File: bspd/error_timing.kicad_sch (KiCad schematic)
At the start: 19 parts, among them Q2 XP262N7002TR-G, Q3 BC856, U6 40106

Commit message: Routing
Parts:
- renumbered D6 to D11, D9 to D12, R35 to R36, R31 to R37, R32 to R38, R33 to R39, R36 to R40, R37 to R41, R38 to R42, R39 to R43
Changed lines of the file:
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@@
 		(on_board yes)
 		(dnp no)
-		(property "Reference" "R35"
+		(property "Reference" "R36"
 			(at 61.595 120.015 90)
 			(effects
@@
 			(project "BSPD"
 				(path "/a7fc0812-140f-4d96-9cd8-ead8c1c610b1/d1e81093-a63e-454a-b453-17bed6f0e773"
-					(reference "R35")
+					(reference "R36")
 					(unit 1)
 				)
@@
 		(on_board yes)
 		(dnp no)
-		(property "Reference" "#PWR066"
+		(property "Reference" "#PWR063"
 			(at 151.765 35.56 0)
 			(effects
@@
 			(project "BSPD"
 				(path "/a7fc0812-140f-4d96-9cd8-ead8c1c610b1/d1e81093-a63e-454a-b453-17bed6f0e773"
-					(reference "#PWR066")
+					(reference "#PWR063")
 					(unit 1)
 				)
@@
 		(on_board yes)
 		(dnp no)
-		(property "Reference" "R36"
+		(property "Reference" "R40"
 			(at 147.32 41.275 0)
 			(effects
@@
 			(project "BSPD"
 				(path "/a7fc0812-140f-4d96-9cd8-ead8c1c610b1/d1e81093-a63e-454a-b453-17bed6f0e773"
-					(reference "R36")
+					(reference "R40")
 					(unit 1)
 				)
@@
 		(on_board yes)
 		(dnp no)
-		(property "Reference" "R37"
+		(property "Reference" "R41"
 			(at 151.765 98.425 90)
 			(effects
@@
 			(project "BSPD"
 				(path "/a7fc0812-140f-4d96-9cd8-ead8c1c610b1/d1e81093-a63e-454a-b453-17bed6f0e773"
-					(reference "R37")
+					(reference "R41")
 					(unit 1)
 				)
@@
 		(on_board yes)
 		(dnp no)
-		(property "Reference" "#PWR067"
+		(property "Reference" "#PWR064"
 			(at 164.465 125.095 0)
 			(effects
@@
 			(project "BSPD"
 				(path "/a7fc0812-140f-4d96-9cd8-ead8c1c610b1/d1e81093-a63e-454a-b453-17bed6f0e773"
-					(reference "#PWR067")
+					(reference "#PWR064")
 					(unit 1)
 				)
@@
 		(on_board yes)
 		(dnp no)
-		(property "Reference" "R31"
+		(property "Reference" "R37"
 			(at 80.01 93.345 90)
 			(effects
@@
 			(project "BSPD"
 				(path "/a7fc0812-140f-4d96-9cd8-ead8c1c610b1/d1e81093-a63e-454a-b453-17bed6f0e773"
-					(reference "R31")
+					(reference "R37")
 					(unit 1)
 				)
@@
 		(on_board yes)
 		(dnp no)
-		(property "Reference" "D6"
+		(property "Reference" "D11"
 			(at 85.09 102.87 0)
 			(effects
@@
 			(project "BSPD"
 				(path "/a7fc0812-140f-4d96-9cd8-ead8c1c610b1/d1e81093-a63e-454a-b453-17bed6f0e773"
-					(reference "D6")
+					(reference "D11")
 					(unit 1)
 				)
@@
 		(on_board yes)
 		(dnp no)
-		(property "Reference" "#PWR064"
+		(property "Reference" "#PWR062"
 			(at 146.05 65.405 0)
 			(effects
@@
 			(project "BSPD"
 				(path "/a7fc0812-140f-4d96-9cd8-ead8c1c610b1/d1e81093-a63e-454a-b453-17bed6f0e773"
-					(reference "#PWR064")
+					(reference "#PWR062")
 					(unit 1)
 				)
@@
 		(on_board yes)
 		(dnp no)
-		(property "Reference" "D9"
+		(property "Reference" "D12"
 			(at 147.955 88.265 0)
 			(effects
@@
 			(project "BSPD"
 				(path "/a7fc0812-140f-4d96-9cd8-ead8c1c610b1/d1e81093-a63e-454a-b453-17bed6f0e773"
-					(reference "D9")
+					(reference "D12")
 					(unit 1)
 				)
@@
 		(on_board yes)
 		(dnp no)
-		(property "Reference" "R39"
+		(property "Reference" "R43"
 			(at 155.575 90.805 90)
 			(effects
@@
 			(project "BSPD"
 				(path "/a7fc0812-140f-4d96-9cd8-ead8c1c610b1/d1e81093-a63e-454a-b453-17bed6f0e773"
-					(reference "R39")
+					(reference "R43")
 					(unit 1)
 				)
@@
 		(on_board yes)
 		(dnp no)
-		(property "Reference" "R38"
+		(property "Reference" "R42"
 			(at 154.305 45.72 90)
 			(effects
@@
 			(project "BSPD"
 				(path "/a7fc0812-140f-4d96-9cd8-ead8c1c610b1/d1e81093-a63e-454a-b453-17bed6f0e773"
-					(reference "R38")
+					(reference "R42")
 					(unit 1)
 				)
@@
 		(on_board yes)
 		(dnp no)
-		(property "Reference" "R32"
+		(property "Reference" "R38"
 			(at 91.44 86.36 90)
 			(effects
@@
 			(project "BSPD"
 				(path "/a7fc0812-140f-4d96-9cd8-ead8c1c610b1/d1e81093-a63e-454a-b453-17bed6f0e773"
-					(reference "R32")
+					(reference "R38")
 					(unit 1)
 				)
@@
 		(on_board yes)
 		(dnp no)
-		(property "Reference" "R33"
+		(property "Reference" "R39"
 			(at 92.71 105.41 90)
 			(effects
@@
 			(project "BSPD"
 				(path "/a7fc0812-140f-4d96-9cd8-ead8c1c610b1/d1e81093-a63e-454a-b453-17bed6f0e773"
-					(reference "R33")
+					(reference "R39")
 					(unit 1)
 				)

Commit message: Layout Complete
TODO:
- Silk
- DRC
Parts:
- renumbered C12 to C11, C11 to C12, D12 to D11, D11 to D12, Q3 to Q2, Q2 to Q3, R44 to R36, R40 to R37, R42 to R38, R38 to R39, R43 to R40, R37 to R41, R41 to R42, R39 to R43, R36 to R44, U6 to U3
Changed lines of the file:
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@@
 		(on_board yes)
 		(dnp no)
-		(property "Reference" "R36"
+		(property "Reference" "R44"
 			(at 61.595 120.015 90)
 			(effects
@@
 			(project "BSPD"
 				(path "/a7fc0812-140f-4d96-9cd8-ead8c1c610b1/d1e81093-a63e-454a-b453-17bed6f0e773"
-					(reference "R36")
+					(reference "R44")
 					(unit 1)
 				)
@@
 		(on_board yes)
 		(dnp no)
-		(property "Reference" "U6"
+		(property "Reference" "U3"
 			(at 123.825 101.6 0)
 			(effects
@@
 			(project "BSPD"
 				(path "/a7fc0812-140f-4d96-9cd8-ead8c1c610b1/d1e81093-a63e-454a-b453-17bed6f0e773"
-					(reference "U6")
+					(reference "U3")
 					(unit 4)
 				)
@@
 		(on_board yes)
 		(dnp no)
-		(property "Reference" "R44"
+		(property "Reference" "R36"
 			(at 161.29 38.1 90)
 			(effects
@@
 			(project "BSPD"
 				(path "/a7fc0812-140f-4d96-9cd8-ead8c1c610b1/d1e81093-a63e-454a-b453-17bed6f0e773"
-					(reference "R44")
+					(reference "R36")
 					(unit 1)
 				)
@@
 		(dnp no)
 		(fields_autoplaced yes)
-		(property "Reference" "Q3"
+		(property "Reference" "Q2"
 			(at 171.45 46.99 0)
 			(effects
@@
 			(project "BSPD"
 				(path "/a7fc0812-140f-4d96-9cd8-ead8c1c610b1/d1e81093-a63e-454a-b453-17bed6f0e773"
-					(reference "Q3")
+					(reference "Q2")
 					(unit 1)
 				)
@@
 		(on_board yes)
 		(dnp no)
-		(property "Reference" "#PWR063"
+		(property "Reference" "#PWR059"
 			(at 151.765 35.56 0)
 			(effects
@@
 			(project "BSPD"
 				(path "/a7fc0812-140f-4d96-9cd8-ead8c1c610b1/d1e81093-a63e-454a-b453-17bed6f0e773"
-					(reference "#PWR063")
+					(reference "#PWR059")
 					(unit 1)
 				)
@@
 		(on_board yes)
 		(dnp no)
-		(property "Reference" "R40"
+		(property "Reference" "R37"
 			(at 147.32 41.275 0)
 			(effects
@@
 			(project "BSPD"
 				(path "/a7fc0812-140f-4d96-9cd8-ead8c1c610b1/d1e81093-a63e-454a-b453-17bed6f0e773"
-					(reference "R40")
+					(reference "R37")
 					(unit 1)
 				)
@@
 		(on_board yes)
 		(dnp no)
-		(property "Reference" "Q2"
+		(property "Reference" "Q3"
 			(at 75.565 112.395 0)
 			(effects
@@
 			(project "BSPD"
 				(path "/a7fc0812-140f-4d96-9cd8-ead8c1c610b1/d1e81093-a63e-454a-b453-17bed6f0e773"
-					(reference "Q2")
+					(reference "Q3")
 					(unit 1)
 				)
@@
 		(on_board yes)
 		(dnp no)
-		(property "Reference" "#PWR061"
+		(property "Reference" "#PWR063"
 			(at 108.585 125.73 0)
 			(effects
@@
 			(project "BSPD"
 				(path "/a7fc0812-140f-4d96-9cd8-ead8c1c610b1/d1e81093-a63e-454a-b453-17bed6f0e773"
-					(reference "#PWR061")
+					(reference "#PWR063")
 					(unit 1)
 				)
@@
 		(on_board yes)
 		(dnp no)
-		(property "Reference" "R41"
+		(property "Reference" "R42"
 			(at 151.765 98.425 90)
 			(effects
@@
 			(project "BSPD"
 				(path "/a7fc0812-140f-4d96-9cd8-ead8c1c610b1/d1e81093-a63e-454a-b453-17bed6f0e773"
-					(reference "R41")
+					(reference "R42")
 					(unit 1)
 				)
@@
 		(on_board yes)
 		(dnp no)
-		(property "Reference" "#PWR064"
+		(property "Reference" "#PWR062"
 			(at 164.465 125.095 0)
 			(effects
@@
 			(project "BSPD"
 				(path "/a7fc0812-140f-4d96-9cd8-ead8c1c610b1/d1e81093-a63e-454a-b453-17bed6f0e773"
-					(reference "#PWR064")
+					(reference "#PWR062")
 					(unit 1)
 				)
@@
 		(on_board yes)
 		(dnp no)
-		(property "Reference" "R37"
+		(property "Reference" "R41"
 			(at 80.01 93.345 90)
 			(effects
@@
 			(project "BSPD"
 				(path "/a7fc0812-140f-4d96-9cd8-ead8c1c610b1/d1e81093-a63e-454a-b453-17bed6f0e773"
-					(reference "R37")
+					(reference "R41")
 					(unit 1)
 				)
@@
 		(on_board yes)
 		(dnp no)
-		(property "Reference" "U6"
+		(property "Reference" "U3"
 			(at 224.79 101.6 0)
 			(effects
@@
 			(project "BSPD"
 				(path "/a7fc0812-140f-4d96-9cd8-ead8c1c610b1/d1e81093-a63e-454a-b453-17bed6f0e773"
-					(reference "U6")
+					(reference "U3")
 					(unit 6)
 				)
@@
 		(on_board yes)
 		(dnp no)
-		(property "Reference" "D11"
+		(property "Reference" "D12"
 			(at 85.09 102.87 0)
 			(effects
@@
 			(project "BSPD"
 				(path "/a7fc0812-140f-4d96-9cd8-ead8c1c610b1/d1e81093-a63e-454a-b453-17bed6f0e773"
-					(reference "D11")
+					(reference "D12")
 					(unit 1)
 				)
@@
 		(on_board yes)
 		(dnp no)
-		(property "Reference" "U6"
+		(property "Reference" "U3"
 			(at 192.405 101.6 0)
 			(effects
@@
 			(project "BSPD"
 				(path "/a7fc0812-140f-4d96-9cd8-ead8c1c610b1/d1e81093-a63e-454a-b453-17bed6f0e773"
-					(reference "U6")
+					(reference "U3")
 					(unit 5)
 				)
@@
 		(on_board yes)
 		(dnp no)
-		(property "Reference" "#PWR062"
+		(property "Reference" "#PWR060"
 			(at 146.05 65.405 0)
 			(effects
@@
 			(project "BSPD"
 				(path "/a7fc0812-140f-4d96-9cd8-ead8c1c610b1/d1e81093-a63e-454a-b453-17bed6f0e773"
-					(reference "#PWR062")
+					(reference "#PWR060")
 					(unit 1)
 				)
@@
 		(on_board yes)
 		(dnp no)
-		(property "Reference" "#PWR059"
+		(property "Reference" "#PWR061"
 			(at 72.39 96.52 0)
 			(effects
@@
 			(project "BSPD"
 				(path "/a7fc0812-140f-4d96-9cd8-ead8c1c610b1/d1e81093-a63e-454a-b453-17bed6f0e773"
-					(reference "#PWR059")
+					(reference "#PWR061")
 					(unit 1)
 				)
@@
 		(on_board yes)
 		(dnp no)
-		(property "Reference" "U6"
+		(property "Reference" "U3"
 			(at 54.61 108.585 0)
 			(effects
@@
 			(project "BSPD"
 				(path "/a7fc0812-140f-4d96-9cd8-ead8c1c610b1/d1e81093-a63e-454a-b453-17bed6f0e773"
-					(reference "U6")
+					(reference "U3")
 					(unit 3)
 				)
@@
 		(on_board yes)
 		(dnp no)
-		(property "Reference" "D12"
+		(property "Reference" "D11"
 			(at 147.955 88.265 0)
 			(effects
@@
 			(project "BSPD"
 				(path "/a7fc0812-140f-4d96-9cd8-ead8c1c610b1/d1e81093-a63e-454a-b453-17bed6f0e773"
-					(reference "D12")
+					(reference "D11")
 					(unit 1)
 				)
@@
 		(on_board yes)
 		(dnp no)
-		(property "Reference" "R43"
+		(property "Reference" "R40"
 			(at 155.575 90.805 90)
 			(effects
@@
 			(project "BSPD"
 				(path "/a7fc0812-140f-4d96-9cd8-ead8c1c610b1/d1e81093-a63e-454a-b453-17bed6f0e773"
-					(reference "R43")
+					(reference "R40")
 					(unit 1)
 				)
@@
 		(on_board yes)
 		(dnp no)
-		(property "Reference" "#PWR060"
+		(property "Reference" "#PWR064"
 			(at 72.39 131.445 0)
 			(effects
@@
 			(project "BSPD"
 				(path "/a7fc0812-140f-4d96-9cd8-ead8c1c610b1/d1e81093-a63e-454a-b453-17bed6f0e773"
-					(reference "#PWR060")
+					(reference "#PWR064")
 					(unit 1)
 				)
@@
 		(on_board yes)
 		(dnp no)
-		(property "Reference" "C12"
+		(property "Reference" "C11"
 			(at 148.59 52.705 0)
 			(effects
@@
 			(project "BSPD"
 				(path "/a7fc0812-140f-4d96-9cd8-ead8c1c610b1/d1e81093-a63e-454a-b453-17bed6f0e773"
-					(reference "C12")
+					(reference "C11")
 					(unit 1)
 				)
@@
 		(on_board yes)
 		(dnp no)
-		(property "Reference" "R42"
+		(property "Reference" "R38"
 			(at 154.305 45.72 90)
 			(effects
@@
 			(project "BSPD"
 				(path "/a7fc0812-140f-4d96-9cd8-ead8c1c610b1/d1e81093-a63e-454a-b453-17bed6f0e773"
-					(reference "R42")
+					(reference "R38")
 					(unit 1)
 				)
@@
 		(on_board yes)
 		(dnp no)
-		(property "Reference" "R38"
+		(property "Reference" "R39"
 			(at 91.44 86.36 90)
 			(effects
@@
 			(project "BSPD"
 				(path "/a7fc0812-140f-4d96-9cd8-ead8c1c610b1/d1e81093-a63e-454a-b453-17bed6f0e773"
-					(reference "R38")
+					(reference "R39")
 					(unit 1)
 				)
@@
 		(on_board yes)
 		(dnp no)
-		(property "Reference" "R39"
+		(property "Reference" "R43"
 			(at 92.71 105.41 90)
 			(effects
@@
 			(project "BSPD"
 				(path "/a7fc0812-140f-4d96-9cd8-ead8c1c610b1/d1e81093-a63e-454a-b453-17bed6f0e773"
-					(reference "R39")
+					(reference "R43")
 					(unit 1)
 				)
@@
 		(on_board yes)
 		(dnp no)
-		(property "Reference" "C11"
+		(property "Reference" "C12"
 			(at 111.125 113.03 0)
 			(effects
@@
 			(project "BSPD"
 				(path "/a7fc0812-140f-4d96-9cd8-ead8c1c610b1/d1e81093-a63e-454a-b453-17bed6f0e773"
-					(reference "C11")
+					(reference "C12")
 					(unit 1)
 				)

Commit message: Mouser BOM
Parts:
- C13, RV3: To Order INV -> TRUE
- R39, R40, R43: To Order TRUE -> INV
- RV4: To Order (none) -> INV

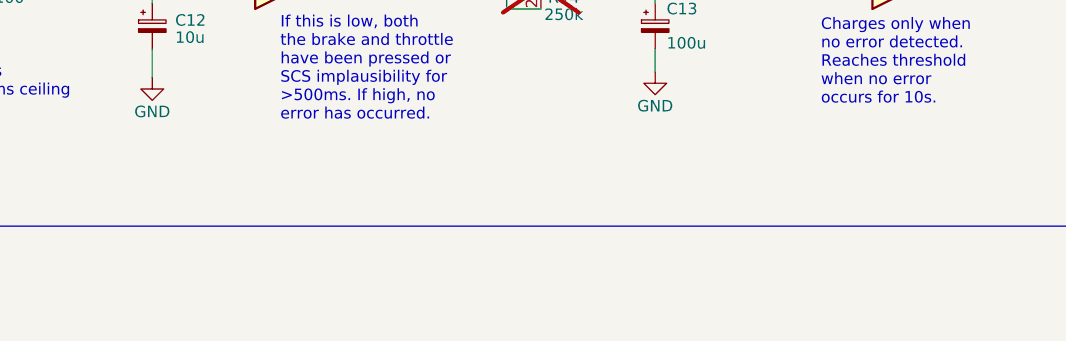
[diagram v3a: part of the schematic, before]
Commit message: Add label for tested BSPD thresholds and timing
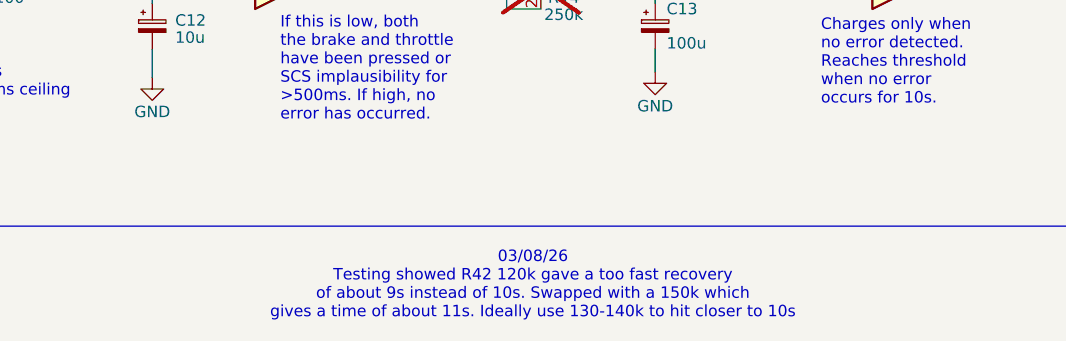
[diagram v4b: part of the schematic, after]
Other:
- note added: "03/08/26 Testing showed R42 120k gave a too fast recovery of about 9s instead of 10s. Swapped with a 150k which gives a time of about 11s. Ideally use 130-140k to hit closer to 10s"
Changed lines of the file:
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@@
+		)
+	)
+	(text "03/08/26\nTesting showed R42 120k gave a too fast recovery\nof about 9s instead of 10s. Swapped with a 150k which\ngives a time of about 11s. Ideally use 130-140k to hit closer to 10s"
+		(exclude_from_sim no)
+		(at 150.876 142.494 0)
+		(effects
+			(font
+				(size 1.27 1.27)
+				(color 255 153 0 1)
+			)
 		)
 	)
